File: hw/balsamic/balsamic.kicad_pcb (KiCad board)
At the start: 4 copper layers, 16.1 x 9.8 mm, 54 parts, among them J1 AXT524124, J3 USB_B_Mini, SW1 SW_Push, U1 ISP1807-LR-RS, U2 BMI160, U3 MAX77651BEWVA+T

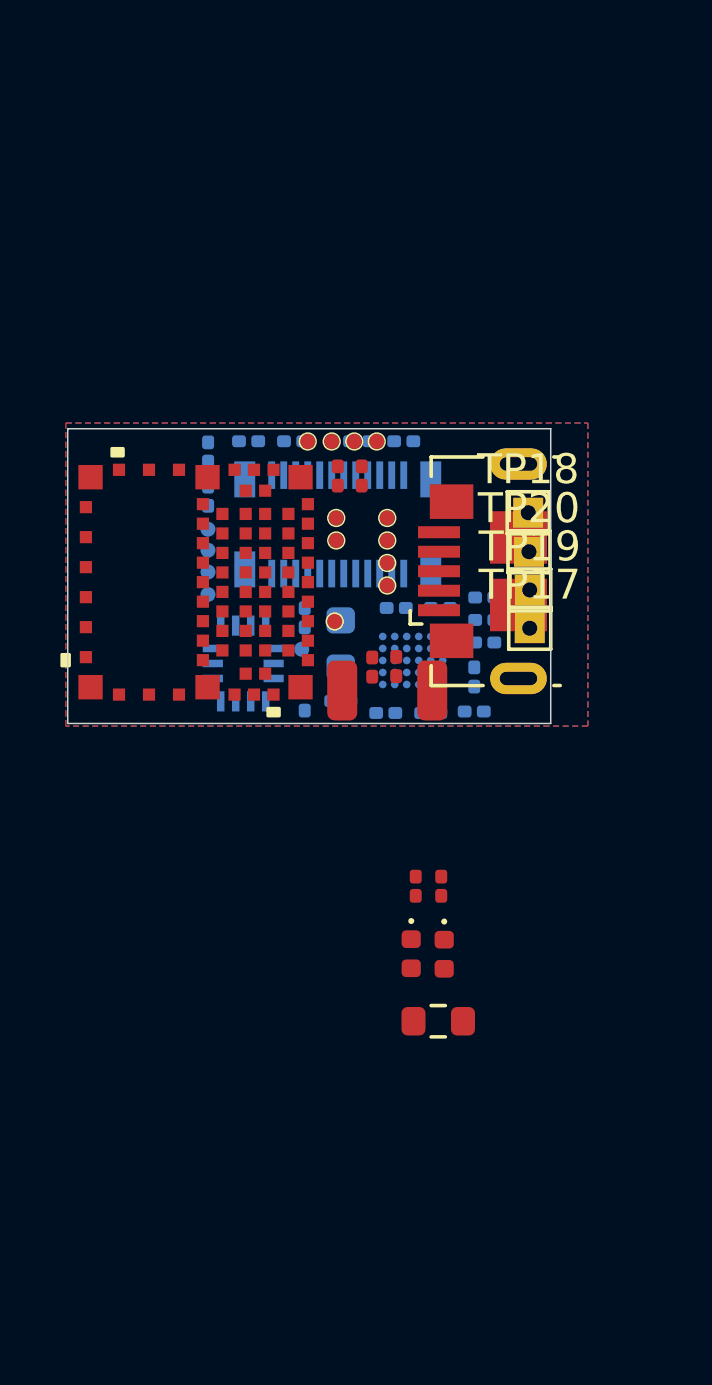
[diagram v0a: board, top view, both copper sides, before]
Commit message: Added symbols and 3D models. Edited schematic
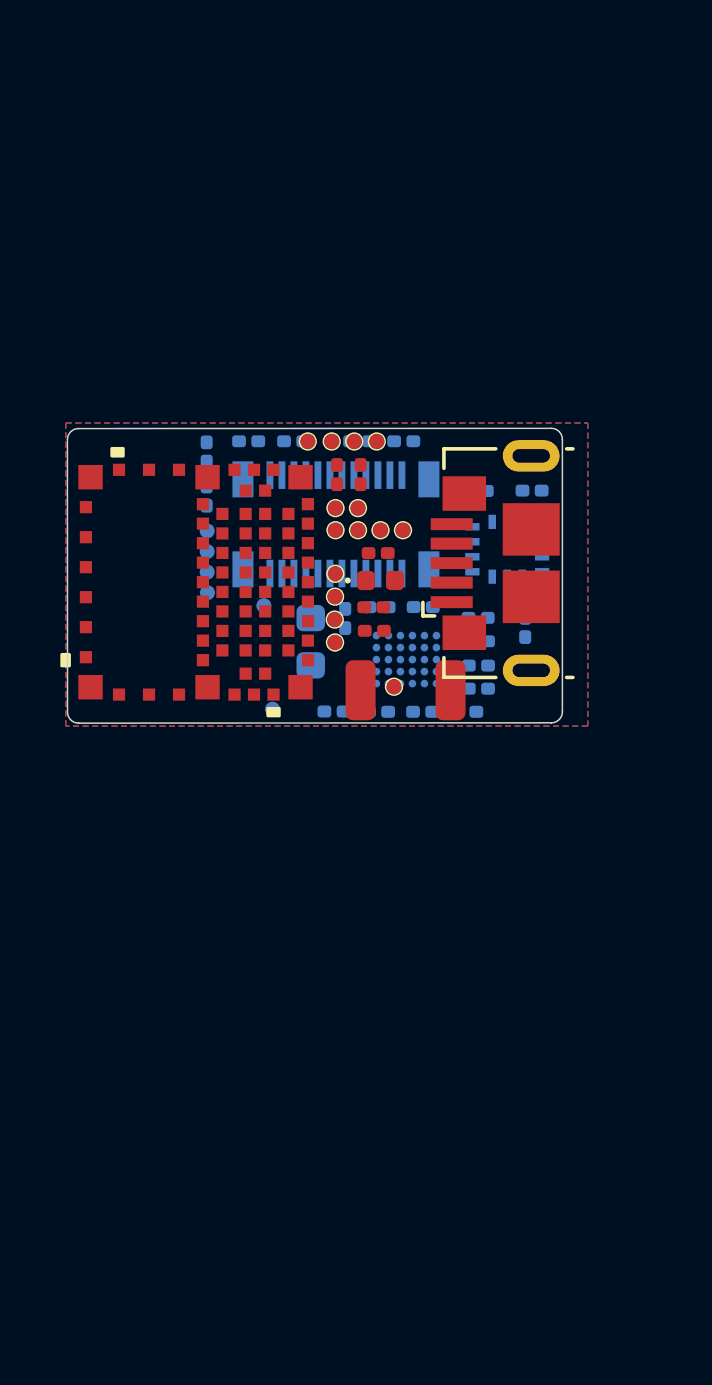
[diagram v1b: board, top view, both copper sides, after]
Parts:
- removed C45: 100nF, Capacitor_SMD:C_0201_0603Metric
- removed the D1 at (75.1, 79.7)
- removed R20: NO_STUFF, Resistor_SMD:R_0201_0603Metric
- removed R33: 200, Resistor_SMD:R_0201_0603Metric
- removed SW1: SW_Push, Resistor_SMD:R_0603_1608Metric
- removed the TP17 at (78.0, 68.9)
- removed the TP18 at (77.9, 65.0)
- removed the TP19 at (78.0, 67.6)
- removed the TP20 at (77.9, 66.3)
- removed the U2 at (68.4, 70.0)
- added C13: 10uF, Capacitor_SMD:C_0201_0603Metric, B.Cu at (71.4, 71.7)
- added C6: 100nF, Capacitor_SMD:C_0201_0603Metric, B.Cu at (76.2, 64.3)
- added R1: NO_STUFF, Resistor_SMD:R_0201_0603Metric, B.Cu at (78.0, 64.3)
- added R2: 10K, Resistor_SMD:R_0201_0603Metric, B.Cu at (77.8, 68.8)
- added TP1: TestPoint, custom_testpoints:TestPoint_Pad_D0.5mm, F.Cu at (71.5, 68.6)
- added TP11: TestPoint, custom_testpoints:TestPoint_Pad_D0.5mm, F.Cu at (71.5, 67.1)
- added TP2: TestPoint, custom_testpoints:TestPoint_Pad_D0.5mm, F.Cu at (71.5, 69.3)
- added TP3: TestPoint, custom_testpoints:TestPoint_Pad_D0.5mm, F.Cu at (73.4, 70.8)
- added TP4: TestPoint, custom_testpoints:TestPoint_Pad_D0.5mm, B.Cu at (69.4, 71.6)
- added U1: BMI270, footprints:XDCR_BMI270, B.Cu at (77.2, 66.2)
- moved D1 12.5 mm to (73.0, 67.3), turned to 0 degrees
- moved R4 11.2 mm to (72.9, 66.4), turned to 0 degrees
- moved C4 2.75 mm to (71.8, 68.5), turned to -90 degrees
- moved C11 2.39 mm to (75.8, 71.7)
- moved R3 2.11 mm to (72.8, 68.2), turned to 180 degrees
- moved TP5 1.92 mm to (69.1, 68.1)
- moved TP12 1.92 mm to (73.7, 65.6), turned to 90 degrees
- moved TP15 1.77 mm to (71.5, 65.6), turned to 90 degrees
- moved TP16 1.30 mm to (72.2, 64.9)
- moved R5 1.21 mm to (72.8, 69.0), turned to 180 degrees
- moved TP13 1.11 mm to (73.0, 65.6), turned to 90 degrees
- moved TP14 1.03 mm to (72.2, 65.6), turned to 90 degrees
- moved L1 1.00 mm to (70.7, 69.3), turned to -90 degrees
- moved TP10 0.83 mm to (71.5, 67.8)
- moved C2 0.77 mm to (76.2, 70.9)
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- renumbered C47 to C10, C7 to C11, C5 to C12, C48 to C14, C49 to C15, C50 to C16, C6 to C17, C12 to C18, C9 to C3, C3 to C4, C10 to C5, C4 to C7, C11 to C9, D2 to D1, J3 to J1, J1 to J2, L2 to L1, R1 to R3, R34 to R4, R2 to R5, R15 to R7, R16 to R8, TP7 to TP10, TP2 to TP12, TP15 to TP13, TP16 to TP14, TP8 to TP15, TP9 to TP16, TP10 to TP17, TP11 to TP18, TP12 to TP19, TP13 to TP20, TP14 to TP21, TP1 to TP5, TP3 to TP6, TP4 to TP7, TP5 to TP8, TP6 to TP9, U3 to U2, U1 to U3
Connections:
- C12 pad 1: PMU_VSBB1 -> PMU_LDO
- J2 pad 18: DVP_D4 -> unconnected-(J2-Pad18)
- J2 pad 20: DVP_D5 -> unconnected-(J2-Pad20)
- J2 pad 22: DVP_D6 -> unconnected-(J2-Pad22)
- J2 pad 24: DVP_D7 -> unconnected-(J2-Pad24)
- U2 pad A2: unconnected-(U3-PadA2) -> Net-(R2-Pad2)
- U2 pad A3: PMU_SDA -> DVP_SDA
- U2 pad B6: PMU_VSBB1 -> PMU_VSBB0
- U2 pad C2: PMU_NIRQ -> unconnected-(U2-PadC2)
- U2 pad C4: PMU_VSBB1 -> PMU_LDO
- U2 pad E6: PMU_VSBB2 -> unconnected-(U2-PadE6)
- U3 pad 3: DVP_SDA -> nRF_P0_12
- U3 pad 35: nRF_P0_05 -> unconnected-(U3-Pad35)
- U3 pad 36: nRF_UART_TX -> unconnected-(U3-Pad36)
- U3 pad 37: unconnected-(U1-Pad37) -> nRF_UART_TX
- U3 pad 38: nRF_P0_03 -> unconnected-(U3-Pad38)
- U3 pad 39: unconnected-(U1-Pad39) -> nRF_UART_RX
- U3 pad 40: nRF_P0_02 -> unconnected-(U3-Pad40)
- U3 pad 42: nRF_P0_31 -> unconnected-(U3-Pad42)
- U3 pad 44: nRF_P0_30 -> unconnected-(U3-Pad44)
- U3 pad 52: nRF_P1_14 -> unconnected-(U3-Pad52)
- U3 pad 53: nRF_P1_13 -> unconnected-(U3-Pad53)
- U3 pad 57: PMU_SDA -> DVP_SDA
- U3 pad 59: nRF_P1_12 -> unconnected-(U3-Pad59)
- U3 pad 60: nRF_P1_10 -> unconnected-(U3-Pad60)
- U3 pad 61: nRF_P1_11 -> unconnected-(U3-Pad61)
- U3 pad 62: PMU_NIRQ -> unconnected-(U3-Pad62)
- U3 pad 63: nRF_P1_04 -> unconnected-(U3-Pad63)
- U3 pad 64: nRF_P1_01 -> unconnected-(U3-Pad64)
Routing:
- removed copper zone on In1.Cu, net GND
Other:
- board size 16.1 x 9.8 mm -> 16.5 x 9.8 mm
- copper layers 4 -> 2

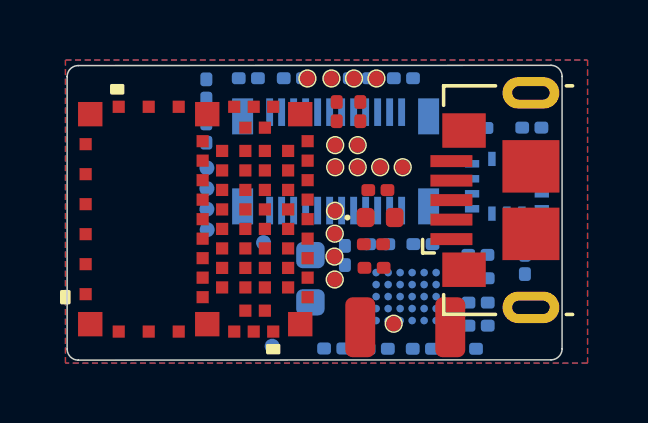
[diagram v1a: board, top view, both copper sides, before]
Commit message: Began 2 layer-routing
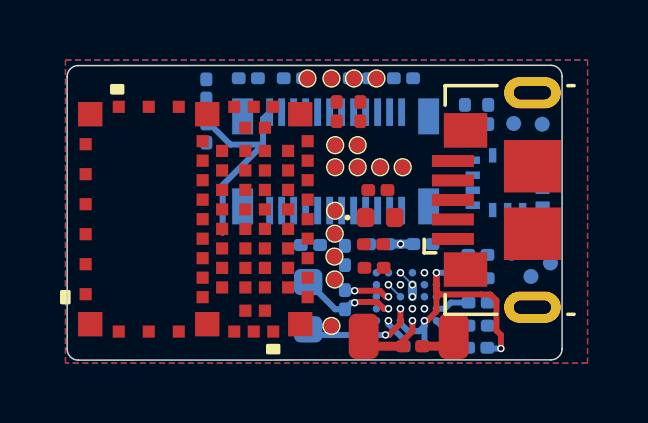
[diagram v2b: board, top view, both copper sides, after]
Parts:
- C7: moved to F.Cu
- moved TP9 11.7 mm to (78.7, 68.0)
- moved TP4 11.7 mm to (78.4, 64.2)
- moved TP8 11.5 mm to (78.7, 68.8)
- moved TP7 11.2 mm to (78.0, 69.2)
- moved TP6 10.3 mm to (77.3, 68.5)
- moved TP5 9.24 mm to (77.4, 64.2)
- moved C9 4.13 mm to (70.7, 68.2)
- moved R2 3.19 mm to (76.2, 71.6), turned to 180 degrees
- moved C13 3.12 mm to (71.8, 68.5), turned to -90 degrees
- moved R1 2.27 mm to (75.8, 63.9), turned to 90 degrees
- moved TP3 2.08 mm to (71.3, 70.9)
- moved C11 1.78 mm to (74.1, 71.6), turned to 180 degrees
- moved C4 1.48 mm to (71.8, 70.0), turned to 90 degrees
- moved L1 0.90 mm to (70.6, 70.2)
- moved C6 0.59 mm to (76.6, 63.9), turned to 90 degrees
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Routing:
- net PMU_VSYS: track 0.00 -> 10.1 mm, vias 0 -> 3
- net PMU_VSBB0: track 0.00 -> 8.09 mm
- net Net-(L1-Pad2): track 0.00 -> 4.16 mm, vias 0 -> 2
- net LXB: track 0.00 -> 3.25 mm, vias 0 -> 2
- net GND: track 0.00 -> 3.19 mm, vias 0 -> 4
- net BATT: track 0.00 -> 2.46 mm, vias 0 -> 1
- net Net-(C4-Pad2): track 0.00 -> 1.54 mm, vias 0 -> 2
- net PMU_LDO: track 0.00 -> 1.40 mm, vias 0 -> 2
- net Net-(C3-Pad1): track 0.00 -> 1.15 mm
- net VBUS_USB: track 0.00 -> 1.15 mm
- net Net-(R5-Pad2): vias 0 -> 1
- net Net-(R3-Pad1): vias 0 -> 1
- net Net-(R2-Pad2): vias 0 -> 1
- net DVP_SCL: vias 0 -> 1

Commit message: Began layout of flex-pcb
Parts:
- removed TP1, TP2, TP3: TestPoint, custom_testpoints:TestPoint_Pad_D0.5mm
- added BT2: GREPOW_Battery, footprints:balsamic_grepow_battery, F.Cu at (76.0, 82.6)
- added D2: LED, LED_SMD:LED_0402_1005Metric, F.Cu at (79.4, 75.5)
- added R6: 200, Resistor_SMD:R_0201_0603Metric, F.Cu at (79.3, 78.0)
- added SW1: SW_SPST, footprints:SW4-SMD-5.2X5.2X1.5MM, F.Cu at (70.7, 77.0)
- C1, C10, C11, C12, C13, C14, C15, C16, C17, C18, C2, C3, C4, C5, C6, C8, C9, J2, L1, R1, R2, TP4, TP5, TP6, TP7, TP8, TP9, U1, U2: moved to F.Cu
- J1: value USB_B_Mini -> 5034800440; footprint Connector_USB:USB_Micro-B_GCT_USB3076-30-A -> footprints:CON_5034800440_MOL
- moved TP8 17.6 mm to (72.8, 52.2), turned to 0 degrees
- moved TP6 16.7 mm to (73.8, 52.2)
- moved TP7 16.6 mm to (73.8, 53.2)
- moved TP9 14.7 mm to (75.2, 53.8), turned to 0 degrees
- moved TP4 14.2 mm to (72.8, 51.1), turned to 0 degrees
- moved TP5 13.5 mm to (73.8, 51.2)
- moved U1 13.1 mm to (78.0, 53.0), turned to -90 degrees
- moved BT1 12.5 mm to (68.0, 82.7)
- moved R1 12.3 mm to (75.7, 51.6), turned to 180 degrees
- moved R4 12.0 mm to (77.8, 77.3)
- moved C6 11.5 mm to (75.7, 52.4), turned to 180 degrees
- moved TP12 11.5 mm to (71.3, 54.4)
- moved TP13 11.5 mm to (70.6, 54.4)
- moved TP14 11.5 mm to (69.8, 54.4)
- moved TP15 11.5 mm to (69.1, 54.4)
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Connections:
- J1 pad 2: nRF_SWDCLK -> nRF_SWDIO
- J1 pad 3: nRF_SWDIO -> nRF_SWDCLK
- U3 pad 33: Button -> nRF_P0_07
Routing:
- net PMU_VSYS: track 10.1 -> 0.00 mm, vias 3 -> 2
- net PMU_VSBB0: track 8.09 -> 0.00 mm
- net Net-(L1-Pad2): track 4.16 -> 0.00 mm, vias 2 -> 1
- net LXB: track 3.25 -> 0.00 mm, vias 2 -> 1
- net GND: track 3.19 -> 0.00 mm
- net BATT: track 2.46 -> 0.00 mm
- net Net-(C4-Pad2): track 1.54 -> 0.00 mm, vias 2 -> 1
- net PMU_LDO: track 1.40 -> 0.00 mm, vias 2 -> 1
- net Net-(C3-Pad1): track 1.15 -> 0.00 mm
- net VBUS_USB: track 1.15 -> 0.00 mm
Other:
- board size 16.5 x 9.8 mm -> 17.7 x 33.5 mm

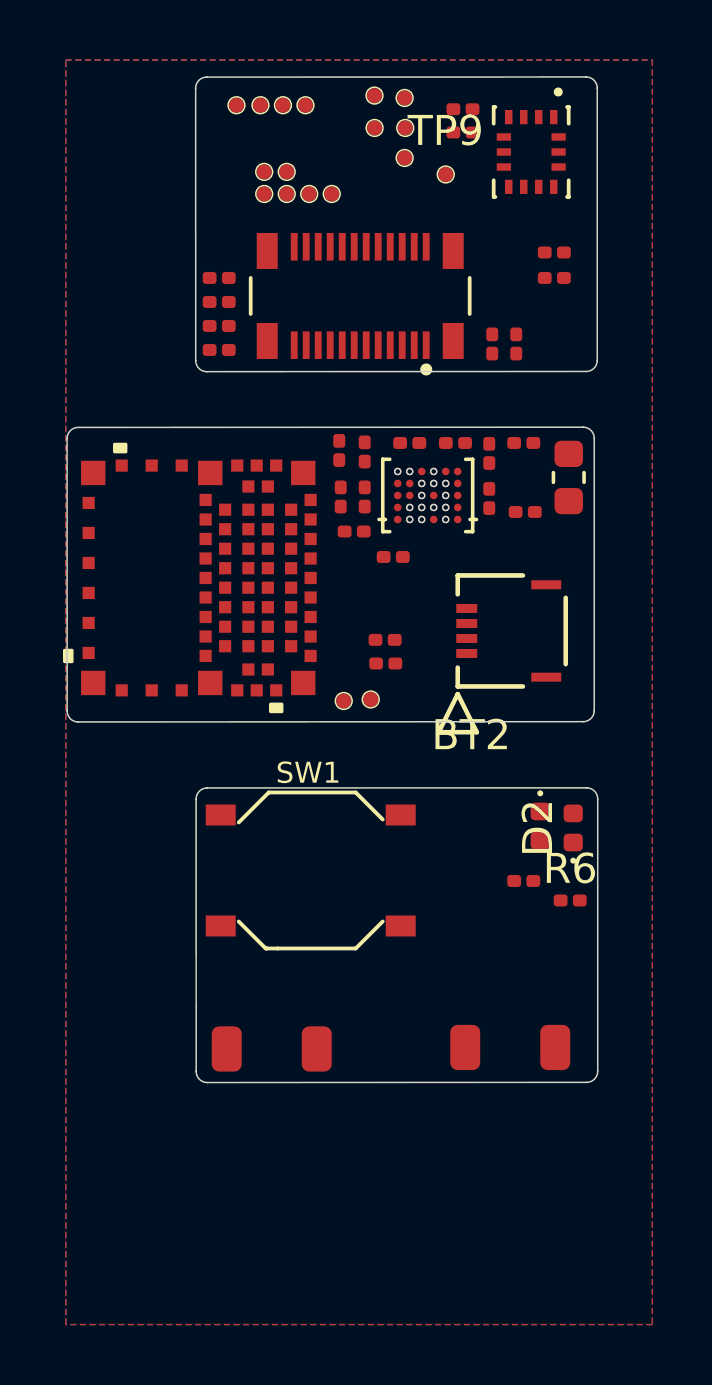
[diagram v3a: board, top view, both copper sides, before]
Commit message: First full routing attempt
- Switched to using a 4 layer board on the islands.
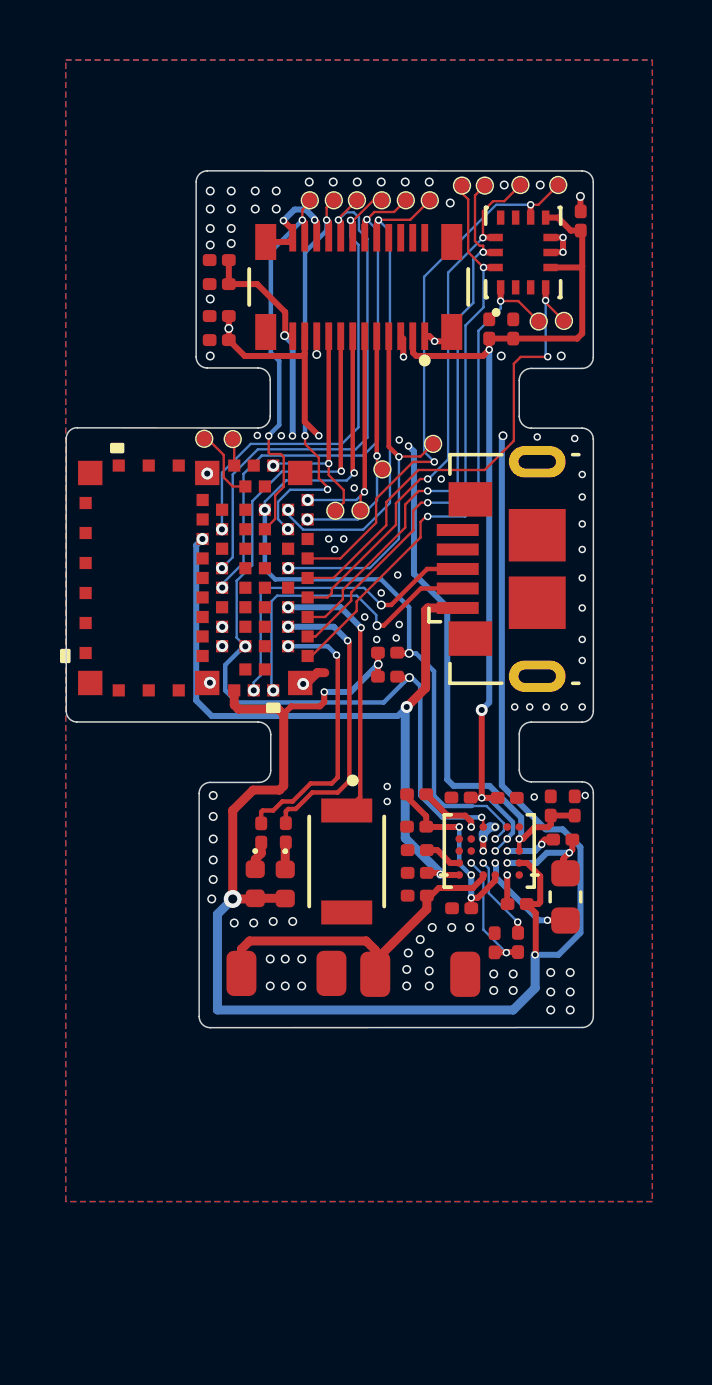
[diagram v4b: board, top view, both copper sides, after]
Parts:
- removed J1: 5034800440, footprints:CON_5034800440_MOL
- removed R1: NO_STUFF, Resistor_SMD:R_0201_0603Metric
- removed SW1: SW_SPST, footprints:SW4-SMD-5.2X5.2X1.5MM
- added J3: USB_B_Micro, Connector_USB:USB_Micro-B_GCT_USB3076-30-A, F.Cu at (77.0, 66.9)
- added S1: B3U-1000P, footprints:SW_B3U-1000P, F.Cu at (71.8, 76.7)
- moved R7 14.5 mm to (73.2, 69.7)
- moved R8 14.4 mm to (73.2, 70.5)
- moved L1 14.0 mm to (79.1, 77.8), turned to -90 degrees
- moved TP18 13.9 mm to (71.5, 65.0)
- moved TP19 13.9 mm to (72.3, 65.0)
- moved C8 13.6 mm to (77.5, 78.1), turned to 180 degrees
- moved C11 13.1 mm to (75.7, 78.2), turned to 180 degrees
- moved C2 12.8 mm to (74.2, 77.0), turned to 180 degrees
- moved C1 12.6 mm to (74.2, 75.5), turned to 180 degrees
- moved TP20 12.6 mm to (73.0, 63.6)
- moved C9 12.2 mm to (79.5, 74.8), turned to 90 degrees
- moved TP21 12.1 mm to (74.7, 62.7)
- moved U2 12.0 mm to (76.6, 76.3)
- moved C5 12.0 mm to (77.2, 74.5)
- moved C12 11.9 mm to (75.7, 74.5)
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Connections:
- C10 pad 2: GNDA -> GND
- C14 pad 1: GNDA -> GND
- C6 pad 1: nRF_P1_06 -> PMU_LDO
- J2 pad 23: GNDA -> GND
- TP10 pad 1: nRF_UART_TX -> nRF_P0_26
- TP11 pad 1: nRF_UART_RX -> nRF_P0_14
- TP4 pad 1: IMU_INT2 -> nRF_P0_31
- TP5 pad 1: IMU_INT1 -> nRF_P0_02
- U1 pad 4: IMU_INT1 -> nRF_P0_02
- U1 pad 5: nRF_P1_06 -> PMU_LDO
- U1 pad 8: nRF_P1_06 -> PMU_LDO
- U1 pad 9: IMU_INT2 -> nRF_P0_31
- U2 pad B1: PMU_GPIO_0 -> unconnected-(U2-PadB1)
- U3 pad 19: IMU_MISO -> unconnected-(U3-Pad19)
- U3 pad 27: IMU_CLK -> unconnected-(U3-Pad27)
- U3 pad 29: IMU_CS -> unconnected-(U3-Pad29)
- U3 pad 3: nRF_P0_12 -> unconnected-(U3-Pad3)
- U3 pad 32: nRF_LED1 -> IMU_MISO
- U3 pad 33: nRF_P0_07 -> nRF_LED1
- U3 pad 34: nRF_LED2 -> IMU_MOSI
- U3 pad 35: unconnected-(U3-Pad35) -> nRF_LED2
- U3 pad 36: unconnected-(U3-Pad36) -> IMU_CLK
- U3 pad 37: nRF_UART_TX -> nRF_P0_15
- U3 pad 38: unconnected-(U3-Pad38) -> IMU_CS
- U3 pad 39: nRF_UART_RX -> unconnected-(U3-Pad39)
- U3 pad 40: unconnected-(U3-Pad40) -> nRF_P0_02
- U3 pad 42: unconnected-(U3-Pad42) -> nRF_P0_31
- U3 pad 49: IMU_INT2 -> unconnected-(U3-Pad49)
- U3 pad 5: unconnected-(U3-Pad5) -> nRF_P0_14
- U3 pad 50: nRF_P1_06 -> unconnected-(U3-Pad50)
- U3 pad 51: IMU_INT1 -> unconnected-(U3-Pad51)
- U3 pad 54: PMU_GPIO_0 -> unconnected-(U3-Pad54)
- U3 pad 58: IMU_MOSI -> unconnected-(U3-Pad58)
- U3 pad 6: unconnected-(U3-Pad6) -> nRF_P0_26
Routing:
- net PMU_VSBB1: track 0.00 -> 69.4 mm, vias 0 -> 7
- net PMU_LDO: track 0.00 -> 31.2 mm, vias 1 -> 5
- net PMU_VSBB0: track 0.00 -> 29.8 mm, vias 0 -> 4
- net DVP_SDA: track 0.00 -> 28.8 mm, vias 0 -> 4
- net DVP_SCL: track 0.00 -> 26.1 mm, vias 1 -> 4
- net VBUS_USB: track 0.00 -> 24.6 mm, vias 0 -> 3
- net IMU_MOSI: track 0.00 -> 19.1 mm, vias 0 -> 2
- net DVP_D2: track 0.00 -> 18.8 mm, vias 0 -> 2
- net IMU_CLK: track 0.00 -> 18.6 mm, vias 0 -> 2
- net nRF_P0_31: track 0.00 -> 18.5 mm, vias 0 -> 2
- net DVP_D0: track 0.00 -> 18.2 mm, vias 0 -> 2
- net IMU_CS: track 0.00 -> 17.9 mm, vias 0 -> 2
- net IMU_MISO: track 0.00 -> 17.3 mm, vias 0 -> 2
- net nRF_P0_02: track 0.00 -> 16.4 mm, vias 0 -> 2
- net DVP_D3: track 0.00 -> 16.4 mm, vias 0 -> 2
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- added copper zone on In1.Cu, net GND
- added copper zone on In2.Cu, net GND
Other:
- board size 17.7 x 33.5 mm -> 17.6 x 28.6 mm
- copper layers 2 -> 4
